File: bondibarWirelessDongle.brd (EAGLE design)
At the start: 38.6 x 56.1 mm, 4 parts

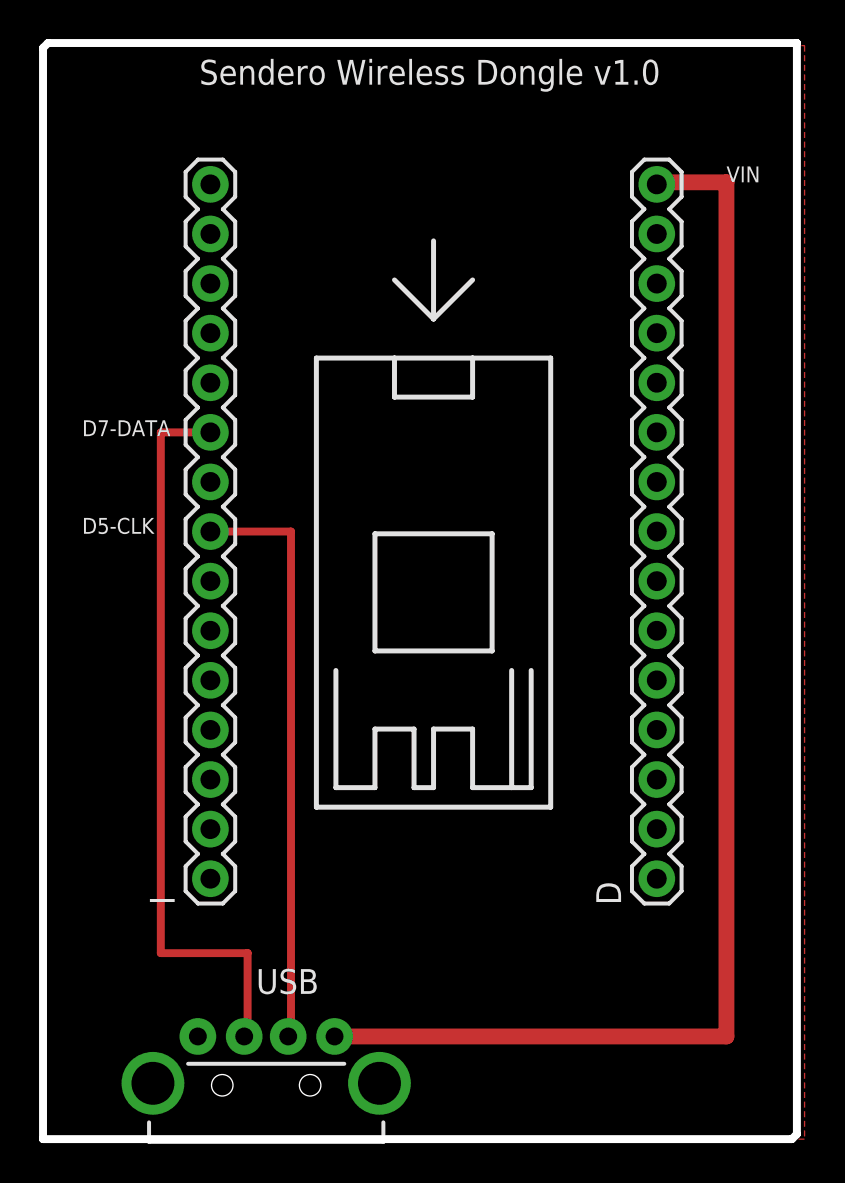
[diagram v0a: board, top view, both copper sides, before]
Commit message: Modified version to print in Seedstudio./
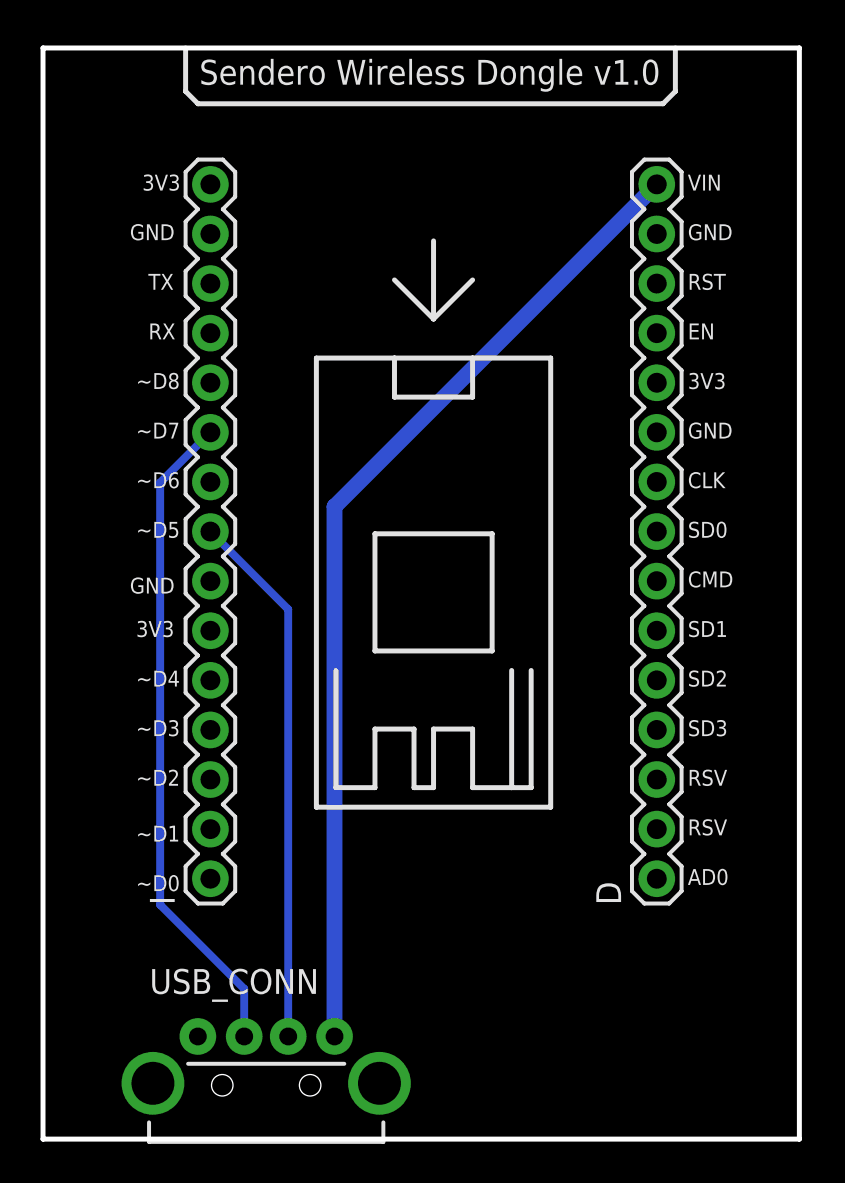
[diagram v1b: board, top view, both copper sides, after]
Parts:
- removed FRAME1: FRAME-LETTERNO_PACKAGE, SparkFun-Aesthetics:DUMMY
- renumbered USB to USB_CONN
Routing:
- net N$2: track 67.6 -> 50.6 mm
- net N$3: track 38.1 -> 33.8 mm
- net N$4: track 30.1 -> 27.5 mm
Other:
- board size 38.6 x 56.1 mm -> 38.7 x 55.9 mm
- board text added: "3V3"
- board text added: "AD0"
- board text added: "CLK"
- board text added: "CMD"
- board text added: "EN"
- board text added: "GND"
- board text added: "RST"
- board text added: "RSV"
- board text added: "RX"
- board text added: "SD0"
- board text added: "SD1"
- board text added: "SD2"
- board text added: "SD3"
- board text added: "TX"
- board text added: "~D0"
- board text added: "~D1"
- board text added: "~D2"
- board text added: "~D3"
- board text added: "~D4"
- board text added: "~D5"
- board text added: "~D6"
- board text added: "~D7"
- board text added: "~D8"
- board text removed: "D5-CLK"
- board text removed: "D7-DATA"
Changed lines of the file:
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@@
 <setting verticaltext="up"/>
 </settings>
-<grid distance="1" unitdist="mm" unit="mm" style="lines" multiple="1" display="yes" altdistance="0.025" altunitdist="inch" altunit="mm"/>
+<grid distance="0.0125" unitdist="inch" unit="inch" style="lines" multiple="1" display="yes" altdistance="0.025" altunitdist="inch" altunit="mm"/>
 <layers>
 <layer number="1" name="Top" color="4" fill="1" visible="yes" active="yes"/>
@@
 <board>
 <plain>
-<wire x1="0" y1="0" x2="38.354" y2="0" width="0.4064" layer="20"/>
-<wire x1="38.354" y1="0" x2="38.608" y2="0.254" width="0.4064" layer="20"/>
-<wire x1="38.608" y1="0.254" x2="38.608" y2="56.134" width="0.4064" layer="20"/>
-<wire x1="38.608" y1="56.134" x2="0.254" y2="56.134" width="0.4064" layer="20"/>
-<wire x1="0.254" y1="56.134" x2="0" y2="55.88" width="0.4064" layer="20"/>
-<wire x1="0" y1="55.88" x2="0" y2="0" width="0.4064" layer="20"/>
-<text x="2" y="31" size="0.8128" layer="21">D5-CLK</text>
-<text x="2" y="36" size="0.8128" layer="21">D7-DATA</text>
-<text x="35" y="49" size="0.8128" layer="21">VIN</text>
 <wire x1="14" y1="40" x2="18" y2="40" width="0.254" layer="21"/>
 <wire x1="18" y1="40" x2="22" y2="40" width="0.254" layer="21"/>
@@
 <wire x1="20" y1="42" x2="22" y2="44" width="0.254" layer="21"/>
 <text x="8" y="54" size="1.27" layer="21">Sendero Wireless Dongle v1.0</text>
+<wire x1="0" y1="0" x2="38.735" y2="0" width="0.254" layer="20"/>
+<wire x1="38.735" y1="0" x2="38.735" y2="55.88" width="0.254" layer="20"/>
+<wire x1="38.735" y1="55.88" x2="0" y2="55.88" width="0.254" layer="20"/>
+<wire x1="0" y1="55.88" x2="0" y2="0" width="0.254" layer="20"/>
+<text x="33.02" y="48.5775" size="0.8128" layer="21">VIN</text>
+<text x="33.02" y="46.0375" size="0.8128" layer="21">GND</text>
+<text x="33.02" y="43.4975" size="0.8128" layer="21">RST</text>
+<text x="33.02" y="40.9575" size="0.8128" layer="21">EN</text>
+<text x="33.02" y="38.4175" size="0.8128" layer="21">3V3</text>
+<text x="33.02" y="35.8775" size="0.8128" layer="21">GND</text>
+<text x="33.02" y="33.3375" size="0.8128" layer="21">CLK</text>
+<text x="33.02" y="30.7975" size="0.8128" layer="21">SD0</text>
+<text x="33.02" y="28.2575" size="0.8128" layer="21">CMD</text>
+<text x="33.02" y="25.7175" size="0.8128" layer="21">SD1</text>
+<text x="33.02" y="23.1775" size="0.8128" layer="21">SD2</text>
+<text x="33.02" y="20.6375" size="0.8128" layer="21">SD3</text>
+<text x="33.02" y="18.0975" size="0.8128" layer="21">RSV</text>
+<text x="33.02" y="15.5575" size="0.8128" layer="21">RSV</text>
+<text x="33.02" y="13.0175" size="0.8128" layer="21">AD0</text>
+<text x="4.7625" y="12.7" size="0.8128" layer="21">~D0</text>
+<text x="4.7625" y="15.24" size="0.8128" layer="21">~D1</text>
+<text x="4.7625" y="18.0975" size="0.8128" layer="21">~D2</text>
+<text x="4.7625" y="20.6375" size="0.8128" layer="21">~D3</text>
+<text x="4.7625" y="23.1775" size="0.8128" layer="21">~D4</text>
+<text x="4.7625" y="25.7175" size="0.8128" layer="21">3V3</text>
+<text x="4.445" y="27.94" size="0.8128" layer="21">GND</text>
+<text x="4.7625" y="30.7975" size="0.8128" layer="21">~D5</text>
+<text x="4.7625" y="33.3375" size="0.8128" layer="21">~D6</text>
+<text x="4.7625" y="35.8775" size="0.8128" layer="21">~D7</text>
+<text x="4.7625" y="38.4175" size="0.8128" layer="21">~D8</text>
+<text x="5.3975" y="40.9575" size="0.8128" layer="21">RX</text>
+<text x="5.3975" y="43.4975" size="0.8128" layer="21">TX</text>
+<text x="4.445" y="46.0375" size="0.8128" layer="21">GND</text>
+<text x="5.08" y="48.5775" size="0.8128" layer="21">3V3</text>
+<wire x1="7.3025" y1="55.88" x2="7.3025" y2="53.6575" width="0.254" layer="21"/>
+<wire x1="7.3025" y1="53.6575" x2="7.9375" y2="53.0225" width="0.254" layer="21"/>
+<wire x1="7.9375" y1="53.0225" x2="31.75" y2="53.0225" width="0.254" layer="21"/>
+<wire x1="31.75" y1="53.0225" x2="32.385" y2="53.6575" width="0.254" layer="21"/>
+<wire x1="32.385" y1="53.6575" x2="32.385" y2="55.88" width="0.254" layer="21"/>
 </plain>
 <attributes>
@@
 </class>
 </classes>
-<designrules name="Fusion_eagle_rule_v1.1">
+<designrules name="SeeedStudio_2layer_DRU_no_angle_20140221">
 <description language="de">&lt;b&gt;EAGLE Design Rules&lt;/b&gt;
 &lt;p&gt;
@@
 </description>
 <param name="layerSetup" value="(1*16)"/>
-<param name="mtCopper" value="0.035mm 0.035mm 0.035mm 0.035mm 0.035mm 0.035mm 0.035mm 0.035mm 0.035mm 0.035mm 0.035mm 0.035mm 0.035mm 0.035mm 0.035mm 0.035mm"/>
-<param name="mtIsolate" value="1.5mm 0.15mm 0.2mm 0.15mm 0.2mm 0.15mm 0.2mm 0.15mm 0.2mm 0.15mm 0.2mm 0.15mm 0.2mm 0.15mm 0.2mm"/>
+<param name="mtCopper" value="0.035mm 0.0175mm 0.035mm 0.035mm 0.035mm 0.035mm 0.035mm 0.035mm 0.035mm 0.035mm 0.035mm 0.035mm 0.035mm 0.035mm 0.0175mm 0.035mm"/>
+<param name="mtIsolate" value="1.5mm 1.1mm 0.2mm 0.15mm 0.2mm 0.15mm 0.2mm 0.15mm 0.2mm 0.15mm 0.2mm 0.15mm 0.2mm 0.15mm 0.2mm"/>
 <param name="mdWireWire" value="6mil"/>
 <param name="mdWirePad" value="6mil"/>
@@
 </autorouter>
 <elements>
-<element name="FRAME1" library="SparkFun-Aesthetics" package="DUMMY" value="FRAME-LETTERNO_PACKAGE" x="3.81" y="0">
-<attribute name="DESIGNER" value="Nobody" x="3.81" y="0" size="1.778" layer="27" display="off"/>
-<attribute name="VERSION" value="v01" x="3.81" y="0" size="1.778" layer="27" display="off"/>
-</element>
 <element name="D" library="SparkFun-Connectors" package="1X15" value="" x="31.4325" y="13.335" rot="R90"/>
 <element name="I" library="SparkFun-Connectors" package="1X15" value="" x="8.5725" y="13.335" rot="R90"/>
-<element name="USB" library="SparkFun-Connectors" package="USB-A-H" value="USB-A-H" x="11.43" y="2.8575" rot="R90">
+<element name="USB_CONN" library="SparkFun-Connectors" package="USB-A-H" value="USB-A-H" x="11.43" y="2.8575" rot="R90">
 <attribute name="PROD_ID" value="CONN-08367" x="11.43" y="2.8575" size="1.778" layer="27" rot="R90" display="off"/>
 </element>
@@
 <signal name="N$3">
 <contactref element="I" pad="10"/>
-<contactref element="USB" pad="D+"/>
-<wire x1="10.303" y1="5.2575" x2="10.4775" y2="5.2575" width="0.4064" layer="1"/>
-<wire x1="10.4775" y1="5.2575" x2="10.4775" y2="9.525" width="0.4064" layer="1"/>
-<wire x1="10.4775" y1="9.525" x2="6.0325" y2="9.525" width="0.4064" layer="1"/>
-<wire x1="6.0325" y1="9.525" x2="6.0325" y2="36.195" width="0.4064" layer="1"/>
-<wire x1="6.0325" y1="36.195" x2="8.5725" y2="36.195" width="0.4064" layer="1"/>
+<contactref element="USB_CONN" pad="D+"/>
+<wire x1="10.303" y1="5.2575" x2="10.303" y2="7.697" width="0.4064" layer="16"/>
+<wire x1="10.303" y1="7.697" x2="6" y2="12" width="0.4064" layer="16"/>
+<wire x1="6" y1="12" x2="6" y2="33.6225" width="0.4064" layer="16"/>
+<wire x1="6" y1="33.6225" x2="8.5725" y2="36.195" width="0.4064" layer="16"/>
 </signal>
 <signal name="N$4">
-<contactref element="USB" pad="D-"/>
+<contactref element="USB_CONN" pad="D-"/>
 <contactref element="I" pad="8"/>
-<wire x1="12.557" y1="5.2575" x2="12.7" y2="5.2575" width="0.4064" layer="1"/>
-<wire x1="12.7" y1="5.2575" x2="12.7" y2="31.115" width="0.4064" layer="1"/>
-<wire x1="12.7" y1="31.115" x2="8.5725" y2="31.115" width="0.4064" layer="1"/>
+<wire x1="12.557" y1="5.2575" x2="12.557" y2="27.1305" width="0.4064" layer="16"/>
+<wire x1="12.557" y1="27.1305" x2="8.5725" y2="31.115" width="0.4064" layer="16"/>
 </signal>
 <signal name="N$2">
-<contactref element="USB" pad="VBUS"/>
+<contactref element="USB_CONN" pad="VBUS"/>
 <contactref element="D" pad="15"/>
 <wire x1="31.4325" y1="49" x2="31.4325" y2="48.895" width="0.6096" layer="16"/>
-<wire x1="14.93" y1="5.2575" x2="35" y2="5.2575" width="0.8128" layer="1"/>
-<wire x1="35" y1="5.2575" x2="35" y2="49" width="0.8128" layer="1"/>
-<wire x1="35" y1="49" x2="31.4325" y2="49" width="0.8128" layer="1"/>
-<wire x1="31.4325" y1="49" x2="31.4325" y2="48.895" width="0.8128" layer="1"/>
+<wire x1="14.93" y1="5.2575" x2="14.93" y2="32.3925" width="0.8128" layer="16"/>
+<wire x1="14.93" y1="32.3925" x2="31.4325" y2="48.895" width="0.8128" layer="16"/>
 </signal>
 <signal name="GND">
-<contactref element="USB" pad="GND"/>
+<contactref element="USB_CONN" pad="GND"/>
 <contactref element="D" pad="14"/>
-<polygon width="0.254" layer="1" isolate="0.3048">
+<polygon width="0.4064" layer="1" isolate="0.3048">
 <vertex x="0" y="0"/>
-<vertex x="0" y="56"/>
-<vertex x="39" y="56"/>
-<vertex x="39" y="0"/>
+<vertex x="0" y="55.88"/>
+<vertex x="38.735" y="55.88"/>
+<vertex x="38.735" y="0"/>
 </polygon>
 </signal>

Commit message: v0.4 - Seedstudio printed version
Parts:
- moved D 2.54 mm to (31.4, 10.8)
- moved I 2.54 mm to (8.57, 10.8)
- renumbered USB_CONN to DATA_OUT
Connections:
- net GND: now also D.10, I.14, I.7
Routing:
- net N$3: track 33.8 -> 31.2 mm
- net N$4: track 27.5 -> 25.0 mm
- net N$2: track 50.6 -> 48.0 mm
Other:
- board size 38.7 x 55.9 mm -> 38.7 x 49.8 mm
